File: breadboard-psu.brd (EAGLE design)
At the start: 42 x 50 mm, 22 parts, among them J1 163-5010-E, J3 5V-CABLE, J5 3.3V-CABLE, K1 GF-126-0159, K2 GF-126-0159, K3 GF-126-0159, U1 AP1117T50G-U, U2 AP1117T33G-U

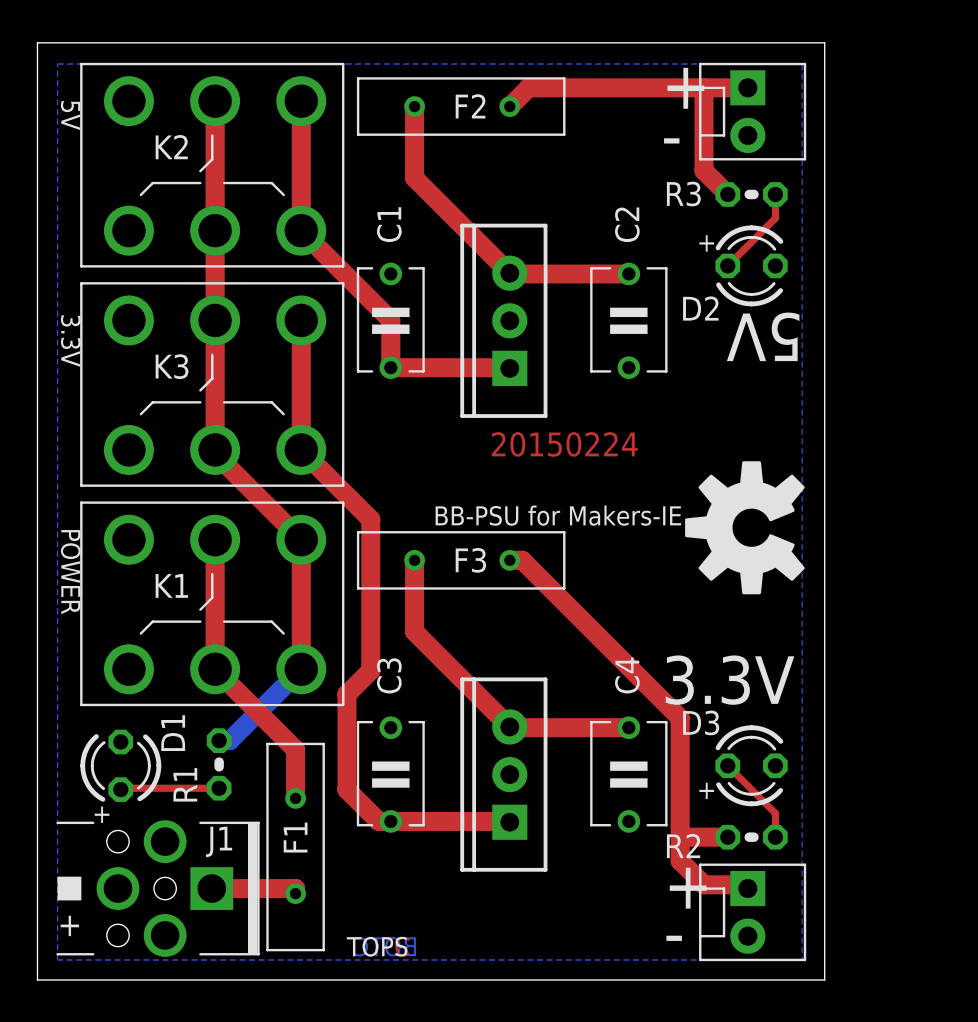
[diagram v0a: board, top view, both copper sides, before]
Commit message: Adjustments after the trial fab run:  - enlarged in X dimension, still fits in 5x5cm  - moved power LED behind DC jack, better contrast and visibility  - enlarged legend text for switches and added signage for the ON position.
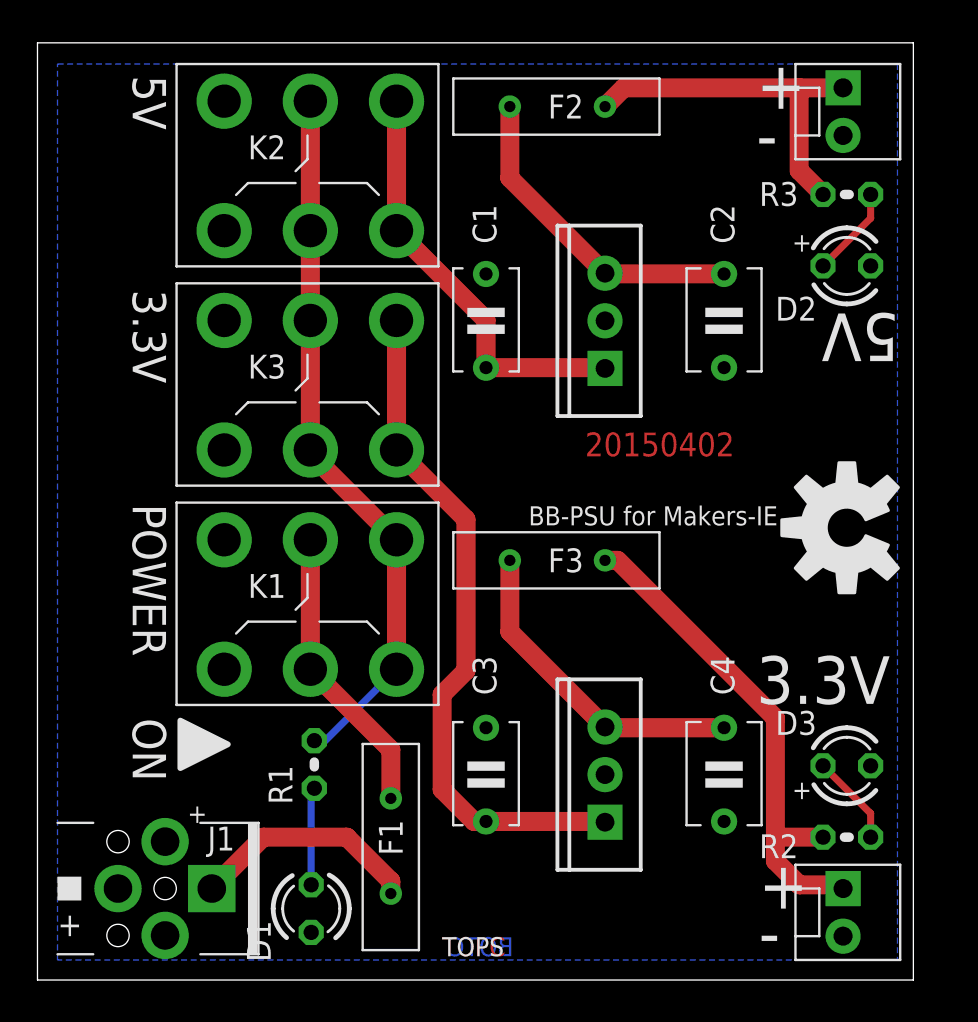
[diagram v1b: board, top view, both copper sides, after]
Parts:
- R1: value 560R -> 560R, 1/2W
- U1: value AP1117T50G-U -> LF50CV
- U2: value AP1117T33G-U -> LF33CV
- moved D1 12.7 mm to (14.6, 3.81), turned to 270 degrees
- moved C2 5.08 mm to (36.6, 35.2)
- moved C4 5.08 mm to (36.6, 11.0)
- moved F1 5.08 mm to (18.9, 7.15)
- moved U1 5.08 mm to (30.3, 35.2)
- moved U2 5.08 mm to (30.3, 11.0)
- moved K1 5.08 mm to (9.96, 16.6)
- moved K2 5.08 mm to (9.96, 40.0)
- moved K3 5.08 mm to (9.96, 28.3)
- moved R1 5.08 mm to (14.8, 11.5)
- moved C1 5.08 mm to (23.9, 35.2)
- moved C3 5.08 mm to (23.9, 11.0)
- moved D2 5.08 mm to (43.2, 38.1)
- moved D3 5.08 mm to (43.2, 11.4)
- moved F2 5.08 mm to (27.7, 46.6)
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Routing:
- net N$1: track 4.74 -> 12.3 mm
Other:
- board size 42 x 50 mm -> 46.7 x 50 mm
- board text added: "20150402"
- board text added: "ON"
- board text removed: "20150224"
